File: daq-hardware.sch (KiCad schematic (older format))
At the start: 18 parts, among them J1 USB_B, J2 Micro_SD_Card_Det_Hirose_DM3AT, Q1 MMDT2222A, SW1 SW1, SW2 SW1, U1 CP2102N-A01-GQFN24, U2 ESP32-WROOM-32D

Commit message: Amended boot pin, moved i2c pullups to main schematic
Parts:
- added R? (x2): 4k7, symbol Device:R
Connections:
- net +3V3: now also R?.1, R?.2
- net GPIO0: no longer Q1.6 (C1), U2.25 (IO0)
- net SDA: now reaches U2.33 (IO21)
- net SDA: now also R?.2
- net SCL: now reaches U2.36 (IO22)
- net SCL: now also R?.1
- net BARO_CS: no longer names the net of U2.6 (IO34)
- new net BOOT: Q1.6 (C1), U2.25 (IO0)
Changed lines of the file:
@@
 RESET
 Text Label 2900 3750 2    50   ~ 0
-GPIO0
+BOOT
 Wire Wire Line
 	5700 2000 5300 2000
@@
 	6900 2000 7200 2000
 Text Label 7200 2000 2    50   ~ 0
-GPIO0
+BOOT
 $Sheet
 S 9450 4750 1050 350
@@
 Wire Wire Line
 	7200 3600 6900 3600
-Wire Wire Line
-	7200 4200 6900 4200
 Text Label 7200 3200 2    50   ~ 0
 SCLK
@@
 Text Label 7200 3600 2    50   ~ 0
 MOSI
-Text Label 7200 4200 2    50   ~ 0
-BARO_CS
 $Comp
 L Device:R_Small R5
@@
 Wire Wire Line
 	10750 2250 10750 2300
+Wire Wire Line
+	6900 3400 7200 3400
+Wire Wire Line
+	6900 3500 7200 3500
+Text Label 7200 3400 2    50   ~ 0
+SDA
+Text Label 7200 3500 2    50   ~ 0
+SCL
+Wire Wire Line
+	9500 3600 9800 3600
+Wire Wire Line
+	9950 3600 10250 3600
+Text Label 9800 3600 2    50   ~ 0
+SDA
+Text Label 10250 3600 2    50   ~ 0
+SCL
+$Comp
+L Device:R R?
+U 1 1 5DB5090D
+P 9500 3300
+F 0 "R?" H 9570 3346 50  0000 L CNN
+F 1 "4k7" H 9570 3255 50  0000 L CNN
+F 2 "" V 9430 3300 50  0001 C CNN
+F 3 "~" H 9500 3300 50  0001 C CNN
+	1    9500 3300
+	1    0    0    -1
+$EndComp
+Wire Wire Line
+	9500 3600 9500 3450
+$Comp
+L Device:R R?
+U 1 1 5DB50914
+P 9950 3300
+F 0 "R?" H 9880 3254 50  0000 R CNN
+F 1 "4k7" H 9880 3345 50  0000 R CNN
+F 2 "" V 9880 3300 50  0001 C CNN
+F 3 "~" H 9950 3300 50  0001 C CNN
+	1    9950 3300
+	-1   0    0    1
+$EndComp
+Wire Wire Line
+	9950 3450 9950 3600
+$Comp
+L power:+3V3 #PWR?
+U 1 1 5DB5091B
+P 9500 3000
+F 0 "#PWR?" H 9500 2850 50  0001 C CNN
+F 1 "+3V3" H 9515 3173 50  0000 C CNN
+F 2 "" H 9500 3000 50  0001 C CNN
+F 3 "" H 9500 3000 50  0001 C CNN
+	1    9500 3000
+	1    0    0    -1
+$EndComp
+$Comp
+L power:+3V3 #PWR?
+U 1 1 5DB50921
+P 9950 3000
+F 0 "#PWR?" H 9950 2850 50  0001 C CNN
+F 1 "+3V3" H 9965 3173 50  0000 C CNN
+F 2 "" H 9950 3000 50  0001 C CNN
+F 3 "" H 9950 3000 50  0001 C CNN
+	1    9950 3000
+	1    0    0    -1
+$EndComp
+Wire Wire Line
+	9950 3000 9950 3150
+Wire Wire Line
+	9500 3000 9500 3150
 $EndSCHEMATC

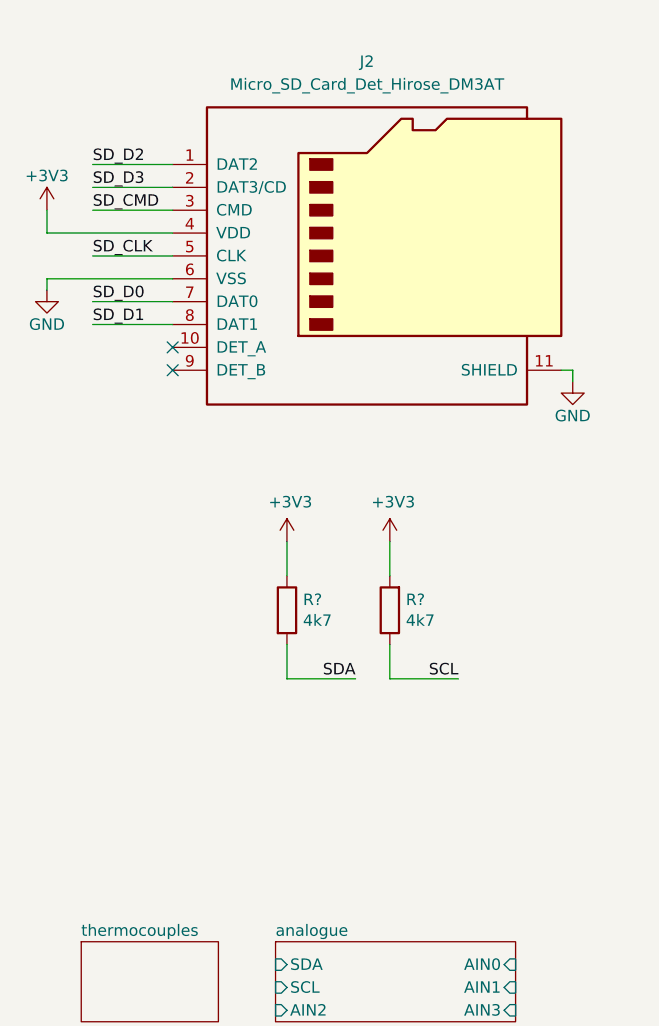
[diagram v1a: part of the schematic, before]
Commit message: Added necessary SDIO pullups
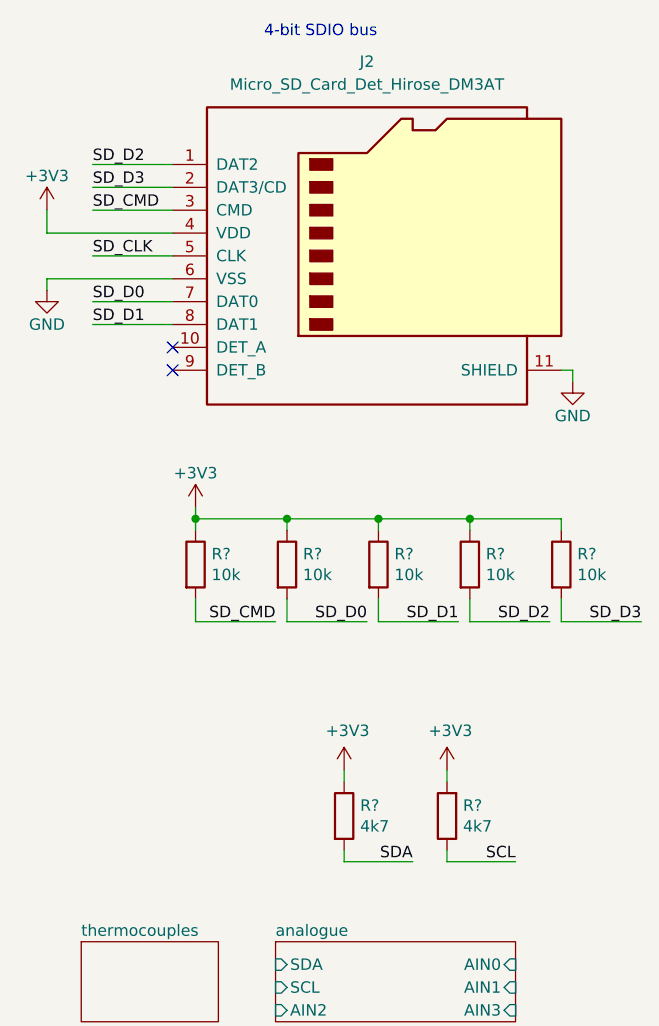
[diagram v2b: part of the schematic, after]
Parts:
- added R? (x5): 10k, symbol Device:R
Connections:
- net +3V3: now also R?.1, R?.1, R?.1, R?.1, R?.1
- net SD_CMD: now also R?.2
- net SD_D0: now also R?.2
- net SD_D1: now also R?.2
- net SD_D2: now also R?.2
- net SD_D3: now also R?.2
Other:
- note added: "4-bit SDIO bus"
- moved on the sheet: R?
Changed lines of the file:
@@
 SCL
 Wire Wire Line
-	9500 3600 9800 3600
-Wire Wire Line
-	9950 3600 10250 3600
-Text Label 9800 3600 2    50   ~ 0
+	9750 4400 10050 4400
+Wire Wire Line
+	10200 4400 10500 4400
+Text Label 10050 4400 2    50   ~ 0
 SDA
-Text Label 10250 3600 2    50   ~ 0
+Text Label 10500 4400 2    50   ~ 0
 SCL
 $Comp
 L Device:R R?
 U 1 1 5DB5090D
-P 9500 3300
-F 0 "R?" H 9570 3346 50  0000 L CNN
-F 1 "4k7" H 9570 3255 50  0000 L CNN
-F 2 "" V 9430 3300 50  0001 C CNN
-F 3 "~" H 9500 3300 50  0001 C CNN
-	1    9500 3300
-	1    0    0    -1
-$EndComp
-Wire Wire Line
-	9500 3600 9500 3450
+P 9750 4200
+AR Path="/5DA926B9/5DB5090D" Ref="R?"  Part="1"
+AR Path="/5DB5090D" Ref="R?"  Part="1"
+F 0 "R?" H 9820 4246 50  0000 L CNN
+F 1 "4k7" H 9820 4155 50  0000 L CNN
+F 2 "" V 9680 4200 50  0001 C CNN
+F 3 "~" H 9750 4200 50  0001 C CNN
+	1    9750 4200
+	1    0    0    -1
+$EndComp
+Wire Wire Line
+	9750 4400 9750 4350
 $Comp
 L Device:R R?
 U 1 1 5DB50914
-P 9950 3300
-F 0 "R?" H 9880 3254 50  0000 R CNN
-F 1 "4k7" H 9880 3345 50  0000 R CNN
-F 2 "" V 9880 3300 50  0001 C CNN
-F 3 "~" H 9950 3300 50  0001 C CNN
-	1    9950 3300
+P 10200 4200
+AR Path="/5DA926B9/5DB50914" Ref="R?"  Part="1"
+AR Path="/5DB50914" Ref="R?"  Part="1"
+F 0 "R?" H 10130 4154 50  0000 R CNN
+F 1 "4k7" H 10130 4245 50  0000 R CNN
+F 2 "" V 10130 4200 50  0001 C CNN
+F 3 "~" H 10200 4200 50  0001 C CNN
+	1    10200 4200
 	-1   0    0    1
 $EndComp
 Wire Wire Line
-	9950 3450 9950 3600
+	10200 4350 10200 4400
 $Comp
 L power:+3V3 #PWR?
 U 1 1 5DB5091B
-P 9500 3000
-F 0 "#PWR?" H 9500 2850 50  0001 C CNN
-F 1 "+3V3" H 9515 3173 50  0000 C CNN
-F 2 "" H 9500 3000 50  0001 C CNN
-F 3 "" H 9500 3000 50  0001 C CNN
-	1    9500 3000
+P 9750 4000
+AR Path="/5DA926B9/5DB5091B" Ref="#PWR?"  Part="1"
+AR Path="/5DB5091B" Ref="#PWR?"  Part="1"
+F 0 "#PWR?" H 9750 3850 50  0001 C CNN
+F 1 "+3V3" H 9765 4173 50  0000 C CNN
+F 2 "" H 9750 4000 50  0001 C CNN
+F 3 "" H 9750 4000 50  0001 C CNN
+	1    9750 4000
 	1    0    0    -1
 $EndComp
@@
 L power:+3V3 #PWR?
 U 1 1 5DB50921
-P 9950 3000
-F 0 "#PWR?" H 9950 2850 50  0001 C CNN
-F 1 "+3V3" H 9965 3173 50  0000 C CNN
-F 2 "" H 9950 3000 50  0001 C CNN
-F 3 "" H 9950 3000 50  0001 C CNN
-	1    9950 3000
-	1    0    0    -1
-$EndComp
-Wire Wire Line
-	9950 3000 9950 3150
-Wire Wire Line
-	9500 3000 9500 3150
+P 10200 4000
+AR Path="/5DA926B9/5DB50921" Ref="#PWR?"  Part="1"
+AR Path="/5DB50921" Ref="#PWR?"  Part="1"
+F 0 "#PWR?" H 10200 3850 50  0001 C CNN
+F 1 "+3V3" H 10215 4173 50  0000 C CNN
+F 2 "" H 10200 4000 50  0001 C CNN
+F 3 "" H 10200 4000 50  0001 C CNN
+	1    10200 4000
+	1    0    0    -1
+$EndComp
+Wire Wire Line
+	10200 4000 10200 4050
+Wire Wire Line
+	9750 4000 9750 4050
+$Comp
+L Device:R R?
+U 1 1 5DB6C1D1
+P 9100 3100
+AR Path="/5DA926B9/5DB6C1D1" Ref="R?"  Part="1"
+AR Path="/5DB6C1D1" Ref="R?"  Part="1"
+F 0 "R?" H 9170 3146 50  0000 L CNN
+F 1 "10k" H 9170 3055 50  0000 L CNN
+F 2 "" V 9030 3100 50  0001 C CNN
+F 3 "~" H 9100 3100 50  0001 C CNN
+	1    9100 3100
+	1    0    0    -1
+$EndComp
+$Comp
+L Device:R R?
+U 1 1 5DB6C807
+P 9500 3100
+AR Path="/5DA926B9/5DB6C807" Ref="R?"  Part="1"
+AR Path="/5DB6C807" Ref="R?"  Part="1"
+F 0 "R?" H 9570 3146 50  0000 L CNN
+F 1 "10k" H 9570 3055 50  0000 L CNN
+F 2 "" V 9430 3100 50  0001 C CNN
+F 3 "~" H 9500 3100 50  0001 C CNN
+	1    9500 3100
+	1    0    0    -1
+$EndComp
+Wire Wire Line
+	9450 3350 9100 3350
+Text Label 9450 3350 2    50   ~ 0
+SD_CMD
+Wire Wire Line
+	9100 3350 9100 3250
+Text Label 9850 3350 2    50   ~ 0
+SD_D0
+Wire Wire Line
+	9500 3350 9500 3250
+Wire Wire Line
+	9850 3350 9500 3350
+Wire Wire Line
+	11050 3350 10700 3350
+Wire Wire Line
+	10700 3350 10700 3250
+Text Label 11050 3350 2    50   ~ 0
+SD_D3
+Wire Wire Line
+	10650 3350 10300 3350
+Wire Wire Line
+	10300 3350 10300 3250
+Text Label 10650 3350 2    50   ~ 0
+SD_D2
+Wire Wire Line
+	10250 3350 9900 3350
+Wire Wire Line
+	9900 3350 9900 3250
+Text Label 10250 3350 2    50   ~ 0
+SD_D1
+$Comp
+L Device:R R?
+U 1 1 5DB6D7EC
+P 10700 3100
+AR Path="/5DA926B9/5DB6D7EC" Ref="R?"  Part="1"
+AR Path="/5DB6D7EC" Ref="R?"  Part="1"
+F 0 "R?" H 10770 3146 50  0000 L CNN
+F 1 "10k" H 10770 3055 50  0000 L CNN
+F 2 "" V 10630 3100 50  0001 C CNN
+F 3 "~" H 10700 3100 50  0001 C CNN
+	1    10700 3100
+	1    0    0    -1
+$EndComp
+$Comp
+L Device:R R?
+U 1 1 5DB6D360
+P 10300 3100
+AR Path="/5DA926B9/5DB6D360" Ref="R?"  Part="1"
+AR Path="/5DB6D360" Ref="R?"  Part="1"
+F 0 "R?" H 10370 3146 50  0000 L CNN
+F 1 "10k" H 10370 3055 50  0000 L CNN
+F 2 "" V 10230 3100 50  0001 C CNN
+F 3 "~" H 10300 3100 50  0001 C CNN
+	1    10300 3100
+	1    0    0    -1
+$EndComp
+$Comp
+L Device:R R?
+U 1 1 5DB6CAE9
+P 9900 3100
+AR Path="/5DA926B9/5DB6CAE9" Ref="R?"  Part="1"
+AR Path="/5DB6CAE9" Ref="R?"  Part="1"
+F 0 "R?" H 9970 3146 50  0000 L CNN
+F 1 "10k" H 9970 3055 50  0000 L CNN
+F 2 "" V 9830 3100 50  0001 C CNN
+F 3 "~" H 9900 3100 50  0001 C CNN
+	1    9900 3100
+	1    0    0    -1
+$EndComp
+$Comp
+L power:+3V3 #PWR?
+U 1 1 5DBA7AD7
+P 9100 2850
+F 0 "#PWR?" H 9100 2700 50  0001 C CNN
+F 1 "+3V3" H 9100 3000 50  0000 C CNN
+F 2 "" H 9100 2850 50  0001 C CNN
+F 3 "" H 9100 2850 50  0001 C CNN
+	1    9100 2850
+	1    0    0    -1
+$EndComp
+Wire Wire Line
+	9100 2850 9100 2900
+Wire Wire Line
+	9100 2900 9500 2900
+Wire Wire Line
+	9500 2900 9500 2950
+Connection ~ 9100 2900
+Wire Wire Line
+	9100 2900 9100 2950
+Wire Wire Line
+	9500 2900 9900 2900
+Wire Wire Line
+	9900 2900 9900 2950
+Connection ~ 9500 2900
+Wire Wire Line
+	9900 2900 10300 2900
+Wire Wire Line
+	10300 2900 10300 2950
+Connection ~ 9900 2900
+Wire Wire Line
+	10300 2900 10700 2900
+Wire Wire Line
+	10700 2900 10700 2950
+Connection ~ 10300 2900
+Text Notes 9400 800  0    50   ~ 0
+4-bit SDIO bus
 $EndSCHEMATC
